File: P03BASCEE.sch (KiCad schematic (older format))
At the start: 13 parts, among them U1 24LC1025, U2 24LC1025, U3 DS13375+, U4 ATMEGA328P-AU, Y1 Crystal 32MHz, Y2 Crystal 16MHz

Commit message: Esquemático completado e passou do DRC
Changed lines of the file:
@@
 $EndComp
 Wire Wire Line
-	3200 3200 3200 3000
+	3200 3200 3200 3100
 Text Label 3200 2050 2    50   ~ 0
 VCC
@@
 	8600 2200 8900 2200
 Wire Wire Line
-	8600 2000 6450 2000
+	8600 2000 7500 2000
 Wire Wire Line
 	6450 2000 6450 2100
@@
 NoConn ~ 5850 3300
 NoConn ~ 5850 3400
+$Comp
+L power:PWR_FLAG #FLG0101
+U 1 1 5F0F4B48
+P 7500 2000
+F 0 "#FLG0101" H 7500 2075 50  0001 C CNN
+F 1 "PWR_FLAG" H 7500 2173 50  0000 C CNN
+F 2 "" H 7500 2000 50  0001 C CNN
+F 3 "~" H 7500 2000 50  0001 C CNN
+	1    7500 2000
+	1    0    0    -1
+$EndComp
+Connection ~ 7500 2000
+Wire Wire Line
+	7500 2000 6450 2000
+$Comp
+L power:PWR_FLAG #FLG0102
+U 1 1 5F0F4DB7
+P 3200 3100
+F 0 "#FLG0102" H 3200 3175 50  0001 C CNN
+F 1 "PWR_FLAG" V 3200 3228 50  0000 L CNN
+F 2 "" H 3200 3100 50  0001 C CNN
+F 3 "~" H 3200 3100 50  0001 C CNN
+	1    3200 3100
+	0    1    1    0
+$EndComp
+Connection ~ 3200 3100
+Wire Wire Line
+	3200 3100 3200 3000
 $EndSCHEMATC

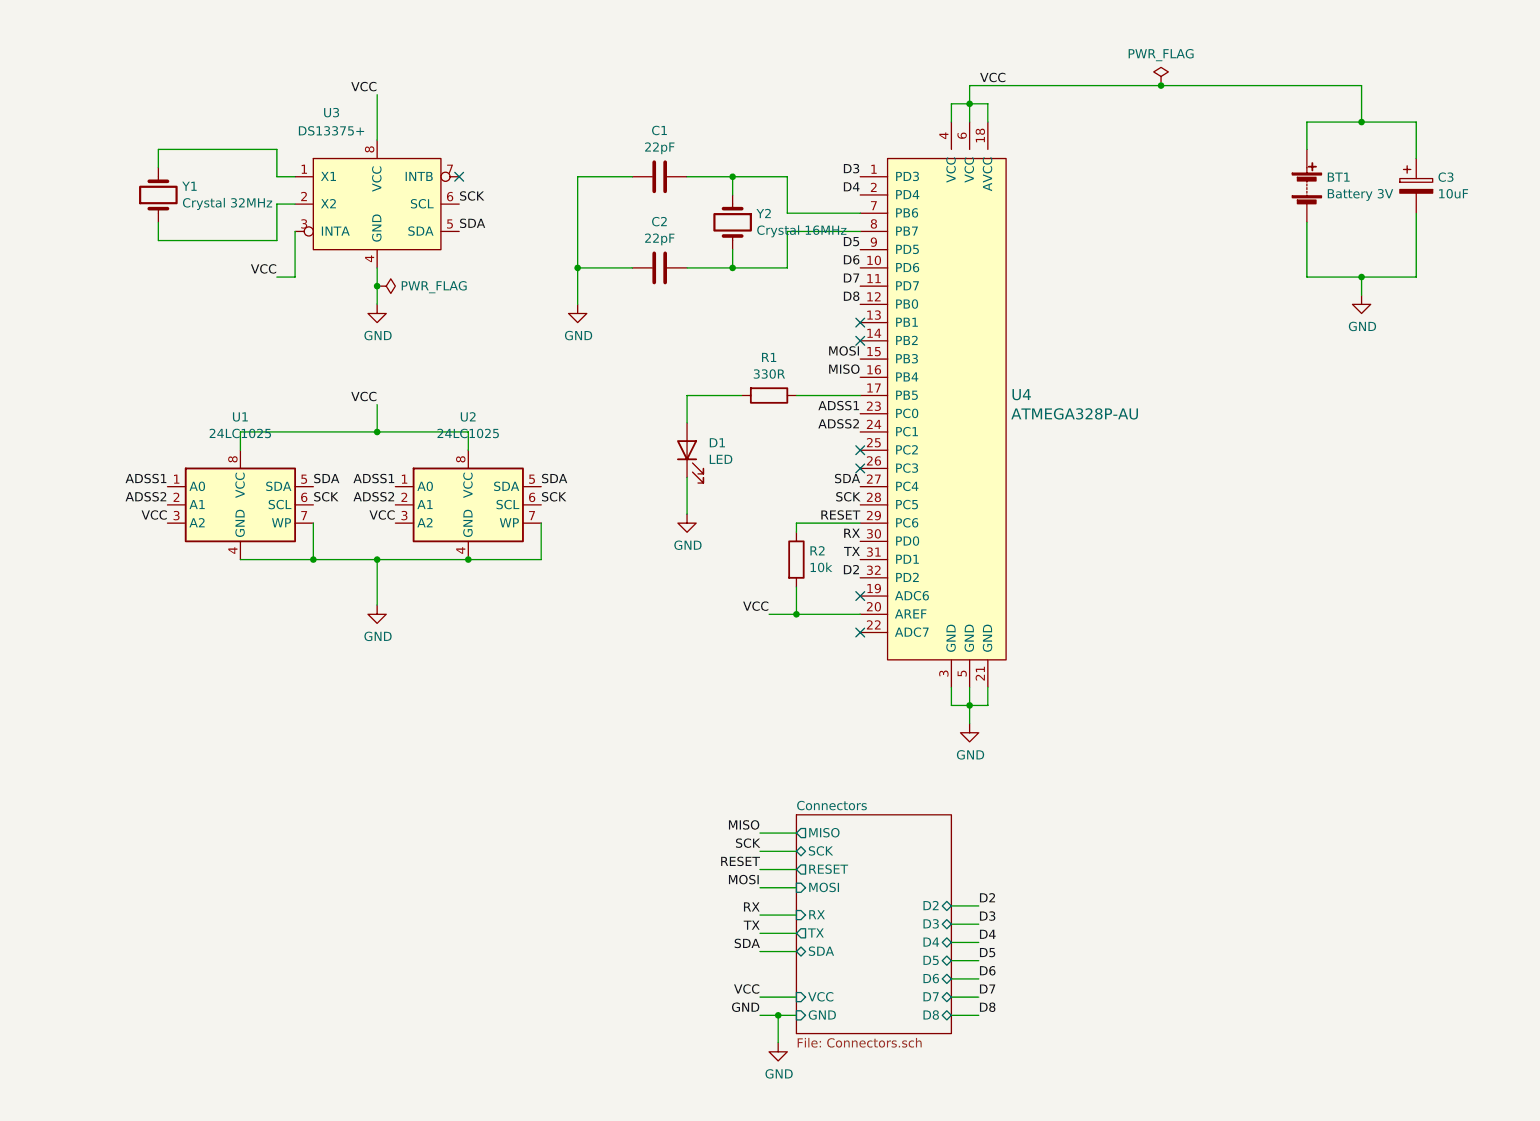
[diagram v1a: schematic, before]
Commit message: Descrições funcionais adicionadas
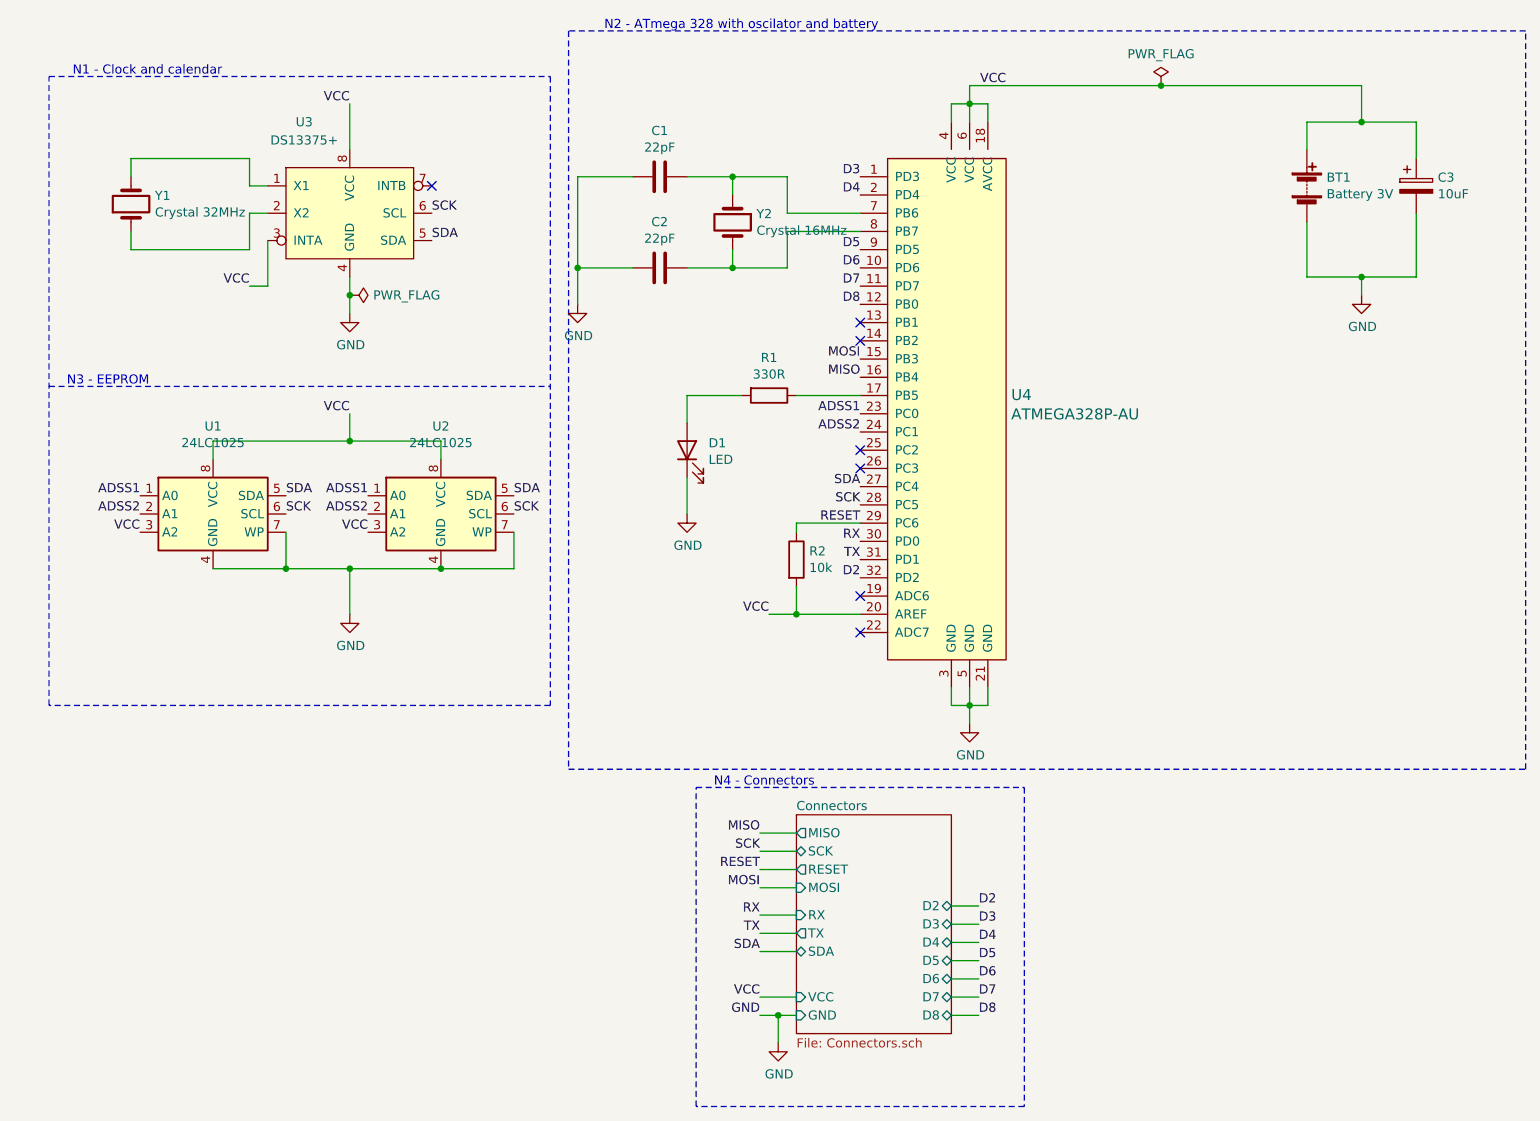
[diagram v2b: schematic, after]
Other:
- note added: "N1 - Clock and calendar"
- note added: "N2 - ATmega 328 with oscilator and battery"
- note added: "N3 - EEPROM"
- note added: "N4 - Connectors"
- moved on the sheet: U1, U2, U3, Y1
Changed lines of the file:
@@
 L Memory_EEPROM:24LC1025 U1
 U 1 1 5F034A3C
-P 2450 4300
-F 0 "U1" H 2450 4781 50  0000 C CNN
-F 1 "24LC1025" H 2450 4690 50  0000 C CNN
-F 2 "Package_SO:SO-8_5.3x6.2mm_P1.27mm" H 2450 4300 50  0001 C CNN
-F 3 "http://ww1.microchip.com/downloads/en/DeviceDoc/21941B.pdf" H 2450 4300 50  0001 C CNN
-	1    2450 4300
+P 2300 4350
+F 0 "U1" H 2300 4831 50  0000 C CNN
+F 1 "24LC1025" H 2300 4740 50  0000 C CNN
+F 2 "Package_SO:SO-8_5.3x6.2mm_P1.27mm" H 2300 4350 50  0001 C CNN
+F 3 "http://ww1.microchip.com/downloads/en/DeviceDoc/21941B.pdf" H 2300 4350 50  0001 C CNN
+	1    2300 4350
 	1    0    0    -1
 $EndComp
@@
 L DS1337:DS1337_PD U3
 U 1 1 5F04ABB9
-P 3200 2650
-F 0 "U3" H 2950 3150 50  0000 C CNN
-F 1 "DS13375+" H 2950 3050 50  0000 C CNN
-F 2 "Package_SO:SO-8_5.3x6.2mm_P1.27mm" H 3200 3050 50  0001 C CNN
-F 3 "https://datasheets.maximintegrated.com/en/ds/DS1337-DS1337C.pdf" H 3200 3050 50  0001 C CNN
-	1    3200 2650
+P 3050 2700
+F 0 "U3" H 2800 3200 50  0000 C CNN
+F 1 "DS13375+" H 2800 3100 50  0000 C CNN
+F 2 "Package_SO:SO-8_5.3x6.2mm_P1.27mm" H 3050 3100 50  0001 C CNN
+F 3 "https://datasheets.maximintegrated.com/en/ds/DS1337-DS1337C.pdf" H 3050 3100 50  0001 C CNN
+	1    3050 2700
 	1    0    0    -1
 $EndComp
@@
 L Device:Crystal Y1
 U 1 1 5F04CD00
-P 2000 2600
-F 0 "Y1" V 2046 2469 50  0000 R CNN
-F 1 "Crystal 32MHz" V 1955 2469 50  0000 R CNN
-F 2 "Crystal:Crystal_SMD_MicroCrystal_CC7V-T1A-2Pin_3.2x1.5mm" H 2000 2600 50  0001 C CNN
-F 3 "~" H 2000 2600 50  0001 C CNN
-	1    2000 2600
+P 1850 2650
+F 0 "Y1" V 1896 2519 50  0000 R CNN
+F 1 "Crystal 32MHz" V 1805 2519 50  0000 R CNN
+F 2 "Crystal:Crystal_SMD_MicroCrystal_CC7V-T1A-2Pin_3.2x1.5mm" H 1850 2650 50  0001 C CNN
+F 3 "~" H 1850 2650 50  0001 C CNN
+	1    1850 2650
 	0    -1   -1   0
 $EndComp
@@
 L Memory_EEPROM:24LC1025 U2
 U 1 1 5F05520E
-P 3700 4300
-F 0 "U2" H 3700 4781 50  0000 C CNN
-F 1 "24LC1025" H 3700 4690 50  0000 C CNN
-F 2 "Package_SO:SO-8_5.3x6.2mm_P1.27mm" H 3700 4300 50  0001 C CNN
-F 3 "http://ww1.microchip.com/downloads/en/DeviceDoc/21941B.pdf" H 3700 4300 50  0001 C CNN
-	1    3700 4300
+P 3550 4350
+F 0 "U2" H 3550 4831 50  0000 C CNN
+F 1 "24LC1025" H 3550 4740 50  0000 C CNN
+F 2 "Package_SO:SO-8_5.3x6.2mm_P1.27mm" H 3550 4350 50  0001 C CNN
+F 3 "http://ww1.microchip.com/downloads/en/DeviceDoc/21941B.pdf" H 3550 4350 50  0001 C CNN
+	1    3550 4350
 	1    0    0    -1
 $EndComp
@@
 	5400 7100 5500 7100
 Wire Wire Line
-	2000 2450 2000 2350
-Wire Wire Line
-	2000 2350 2650 2350
-Wire Wire Line
-	2650 2350 2650 2500
-Wire Wire Line
-	2650 2500 2750 2500
-Wire Wire Line
-	2000 2750 2000 2850
-Wire Wire Line
-	2000 2850 2650 2850
-Wire Wire Line
-	2650 2850 2650 2650
-Wire Wire Line
-	2650 2650 2750 2650
+	1850 2500 1850 2400
+Wire Wire Line
+	1850 2400 2500 2400
+Wire Wire Line
+	2500 2400 2500 2550
+Wire Wire Line
+	2500 2550 2600 2550
+Wire Wire Line
+	1850 2800 1850 2900
+Wire Wire Line
+	1850 2900 2500 2900
+Wire Wire Line
+	2500 2900 2500 2700
+Wire Wire Line
+	2500 2700 2600 2700
 $Comp
 L power:GND #PWR0103
 U 1 1 5F097F67
-P 3200 3200
-F 0 "#PWR0103" H 3200 2950 50  0001 C CNN
-F 1 "GND" H 3205 3027 50  0000 C CNN
-F 2 "" H 3200 3200 50  0001 C CNN
-F 3 "" H 3200 3200 50  0001 C CNN
-	1    3200 3200
-	1    0    0    -1
-$EndComp
-Wire Wire Line
-	3200 3200 3200 3100
-Text Label 3200 2050 2    50   ~ 0
-VCC
-Wire Wire Line
-	3200 2050 3200 2300
-Text Label 2650 3050 2    50   ~ 0
-VCC
-Wire Wire Line
-	2650 3050 2750 3050
-Wire Wire Line
-	2750 3050 2750 2800
-NoConn ~ 3650 2500
-Text Label 3650 2650 0    50   ~ 0
+P 3050 3250
+F 0 "#PWR0103" H 3050 3000 50  0001 C CNN
+F 1 "GND" H 3055 3077 50  0000 C CNN
+F 2 "" H 3050 3250 50  0001 C CNN
+F 3 "" H 3050 3250 50  0001 C CNN
+	1    3050 3250
+	1    0    0    -1
+$EndComp
+Wire Wire Line
+	3050 3250 3050 3150
+Text Label 3050 2100 2    50   ~ 0
+VCC
+Wire Wire Line
+	3050 2100 3050 2350
+Text Label 2500 3100 2    50   ~ 0
+VCC
+Wire Wire Line
+	2500 3100 2600 3100
+Wire Wire Line
+	2600 3100 2600 2850
+NoConn ~ 3500 2550
+Text Label 3500 2700 0    50   ~ 0
 SCK
-Text Label 3650 2800 0    50   ~ 0
+Text Label 3500 2850 0    50   ~ 0
 SDA
-Text Label 3200 3750 2    50   ~ 0
-VCC
-Wire Wire Line
-	3700 3900 3700 4000
+Text Label 3050 3800 2    50   ~ 0
+VCC
+Wire Wire Line
+	3550 3950 3550 4050
 $Comp
 L power:GND #PWR0104
 U 1 1 5F0A9793
-P 3200 4850
-F 0 "#PWR0104" H 3200 4600 50  0001 C CNN
-F 1 "GND" H 3205 4677 50  0000 C CNN
-F 2 "" H 3200 4850 50  0001 C CNN
-F 3 "" H 3200 4850 50  0001 C CNN
-	1    3200 4850
-	1    0    0    -1
-$EndComp
-Wire Wire Line
-	3200 4600 3200 4850
-Wire Wire Line
-	3200 4600 3700 4600
-Connection ~ 3200 4600
-Wire Wire Line
-	3200 3750 3200 3900
-Wire Wire Line
-	3200 3900 3700 3900
-Wire Wire Line
-	4100 4400 4100 4600
-Wire Wire Line
-	4100 4600 3700 4600
-Connection ~ 3700 4600
-Text Label 2050 4400 2    50   ~ 0
-VCC
-Text Label 3300 4400 2    50   ~ 0
-VCC
-Text Label 4100 4200 0    50   ~ 0
+P 3050 4900
+F 0 "#PWR0104" H 3050 4650 50  0001 C CNN
+F 1 "GND" H 3055 4727 50  0000 C CNN
+F 2 "" H 3050 4900 50  0001 C CNN
+F 3 "" H 3050 4900 50  0001 C CNN
+	1    3050 4900
+	1    0    0    -1
+$EndComp
+Wire Wire Line
+	3050 4650 3050 4900
+Wire Wire Line
+	3050 4650 3550 4650
+Connection ~ 3050 4650
+Wire Wire Line
+	3050 3800 3050 3950
+Wire Wire Line
+	3050 3950 3550 3950
+Wire Wire Line
+	3950 4450 3950 4650
+Wire Wire Line
+	3950 4650 3550 4650
+Connection ~ 3550 4650
+Text Label 1900 4450 2    50   ~ 0
+VCC
+Text Label 3150 4450 2    50   ~ 0
+VCC
+Text Label 3950 4250 0    50   ~ 0
 SDA
-Text Label 2850 4200 0    50   ~ 0
+Text Label 2700 4250 0    50   ~ 0
 SDA
-Text Label 4100 4300 0    50   ~ 0
+Text Label 3950 4350 0    50   ~ 0
 SCK
-Text Label 2850 4300 0    50   ~ 0
+Text Label 2700 4350 0    50   ~ 0
 SCK
 Wire Wire Line
-	2450 4600 2850 4600
-Wire Wire Line
-	2850 4400 2850 4600
-Connection ~ 2850 4600
-Wire Wire Line
-	2850 4600 3200 4600
-Wire Wire Line
-	2450 4000 2450 3900
-Wire Wire Line
-	2450 3900 3200 3900
-Connection ~ 3200 3900
-Text Label 2050 4200 2    50   ~ 0
+	2300 4650 2700 4650
+Wire Wire Line
+	2700 4450 2700 4650
+Connection ~ 2700 4650
+Wire Wire Line
+	2700 4650 3050 4650
+Wire Wire Line
+	2300 4050 2300 3950
+Wire Wire Line
+	2300 3950 3050 3950
+Connection ~ 3050 3950
+Text Label 1900 4250 2    50   ~ 0
 ADSS1
-Text Label 2050 4300 2    50   ~ 0
+Text Label 1900 4350 2    50   ~ 0
 ADSS2
-Text Label 3300 4300 2    50   ~ 0
+Text Label 3150 4350 2    50   ~ 0
 ADSS2
-Text Label 3300 4200 2    50   ~ 0
+Text Label 3150 4250 2    50   ~ 0
 ADSS1
 Text Label 5850 3800 2    50   ~ 0
@@
 L power:PWR_FLAG #FLG0102
 U 1 1 5F0F4DB7
-P 3200 3100
-F 0 "#FLG0102" H 3200 3175 50  0001 C CNN
-F 1 "PWR_FLAG" V 3200 3228 50  0000 L CNN
-F 2 "" H 3200 3100 50  0001 C CNN
-F 3 "~" H 3200 3100 50  0001 C CNN
-	1    3200 3100
+P 3050 3150
+F 0 "#FLG0102" H 3050 3225 50  0001 C CNN
+F 1 "PWR_FLAG" V 3050 3278 50  0000 L CNN
+F 2 "" H 3050 3150 50  0001 C CNN
+F 3 "~" H 3050 3150 50  0001 C CNN
+	1    3050 3150
 	0    1    1    0
 $EndComp
-Connection ~ 3200 3100
-Wire Wire Line
-	3200 3100 3200 3000
+Connection ~ 3050 3150
+Wire Wire Line
+	3050 3150 3050 3050
+Wire Notes Line
+	1400 1950 4150 1950
+Wire Notes Line
+	4150 1950 4150 5400
+Wire Notes Line
+	4150 5400 1400 5400
+Wire Notes Line
+	1400 5400 1400 1950
+Wire Notes Line
+	1400 3650 4150 3650
+Wire Notes Line
+	4950 5850 6750 5850
+Wire Notes Line
+	6750 5850 6750 7600
+Wire Notes Line
+	6750 7600 4950 7600
+Wire Notes Line
+	4950 7600 4950 5850
+Wire Notes Line
+	4250 1700 4250 5750
+Wire Notes Line
+	4250 5750 9500 5750
+Wire Notes Line
+	9500 5750 9500 1700
+Wire Notes Line
+	9500 1700 4250 1700
+Text Notes 2350 1950 2    50   ~ 0
+N1 - Clock and calendar
+Text Notes 1950 3650 2    50   ~ 0
+N3 - EEPROM
+Text Notes 5950 1700 2    50   ~ 0
+N2 - ATmega 328 with oscilator and battery
+Text Notes 5600 5850 2    50   ~ 0
+N4 - Connectors
 $EndSCHEMATC
